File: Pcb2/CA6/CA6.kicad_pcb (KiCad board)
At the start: 2 copper layers, 81.3 x 134.6 mm, 115 parts, among them J1 MICRO_USB, J2 BAT_CON, J3 MODULE_0, J4 MODULE_2, J5 MODULE_1, J6 AUX, J7 AUX, J8 MODULE_3, P1 JTAG, P2 RFD22301 Breakout, Q1 BSS138P, Q10 BSS138P, Q11 BSS138P, Q12 BSS138P, Q13 BSS138P, Q14 BSS138P, Q15 BSS138P, Q16 BSS138P, Q2 BSS138P, Q3 BSS138P, Q4 BSS138P, Q5 BSS138P, Q6 BSS138P, Q7 BSS138P, Q8 BSS138P, Q9 BSS138P, SW1 ERASE, SW2 USB/BATTERY, SW3 RESET, U12 VREG_33, U14 EEPROM, U15 L_PIPE, U16 ATSAM3X8EA-AU_LQFP-144, U17 RFD22301, X1 HOLE, X2 HOLE, X3 HOLE, X7 CRYSTAL_4, X8 32khz

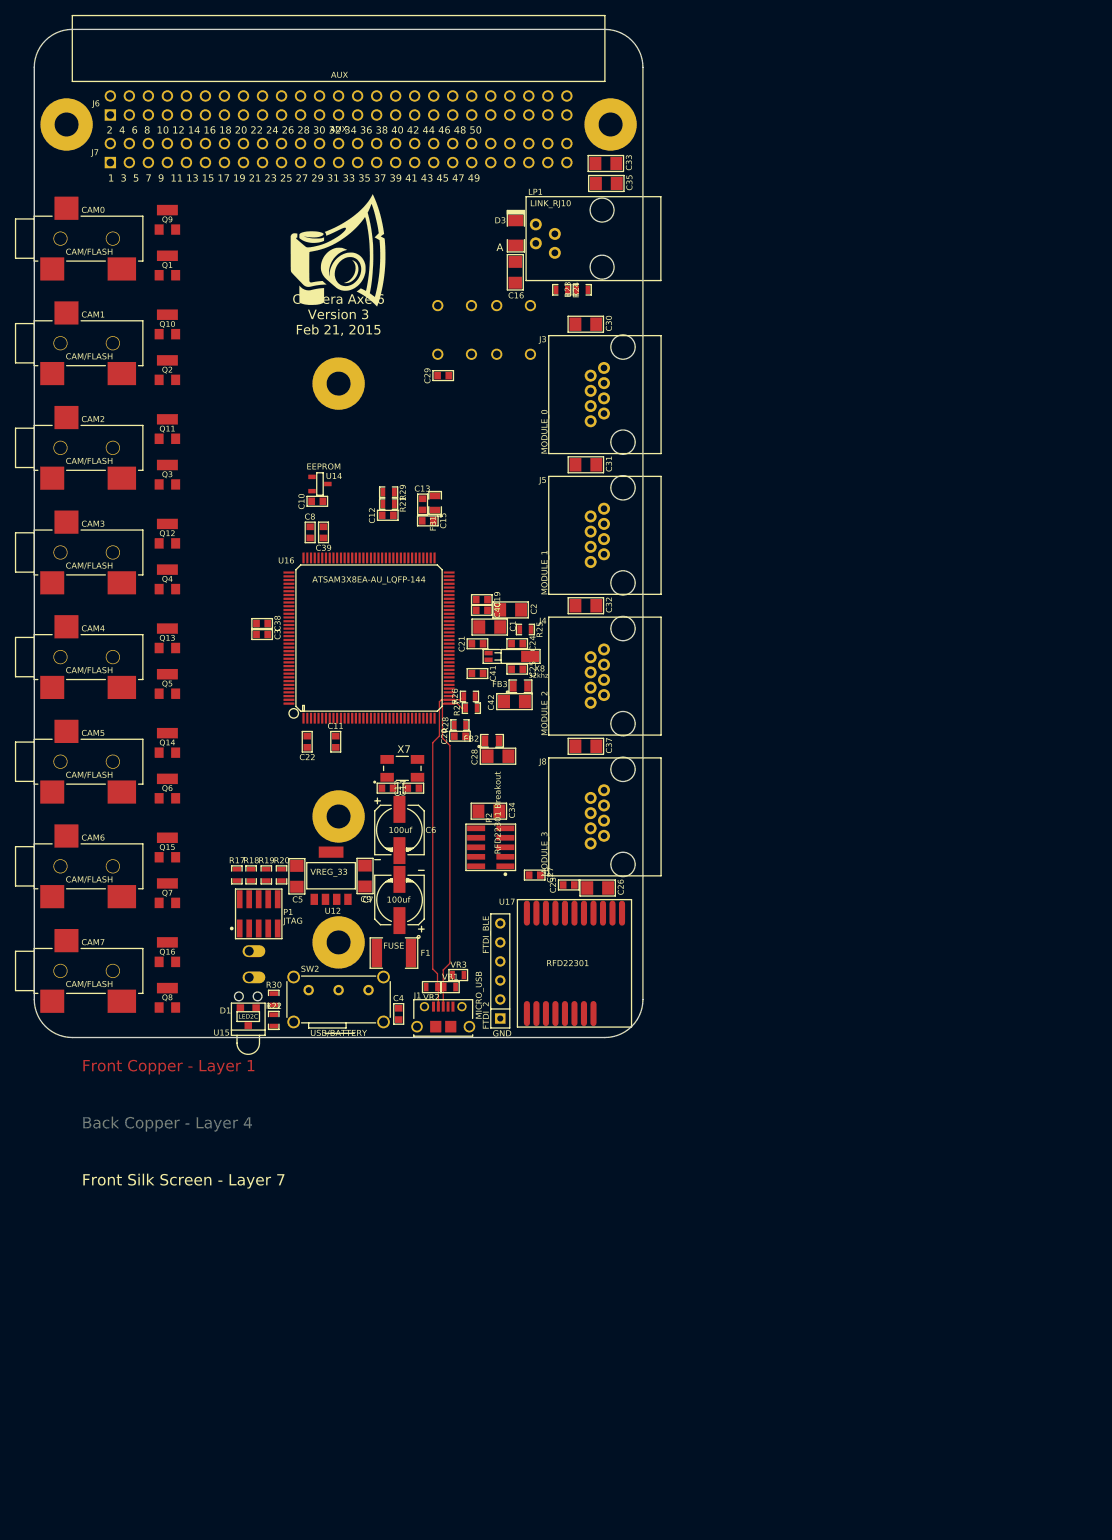
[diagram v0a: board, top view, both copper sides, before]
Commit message: Remove link port, only support 3.3V on aux, make board bigger, make board 2 layers, add camera port leds
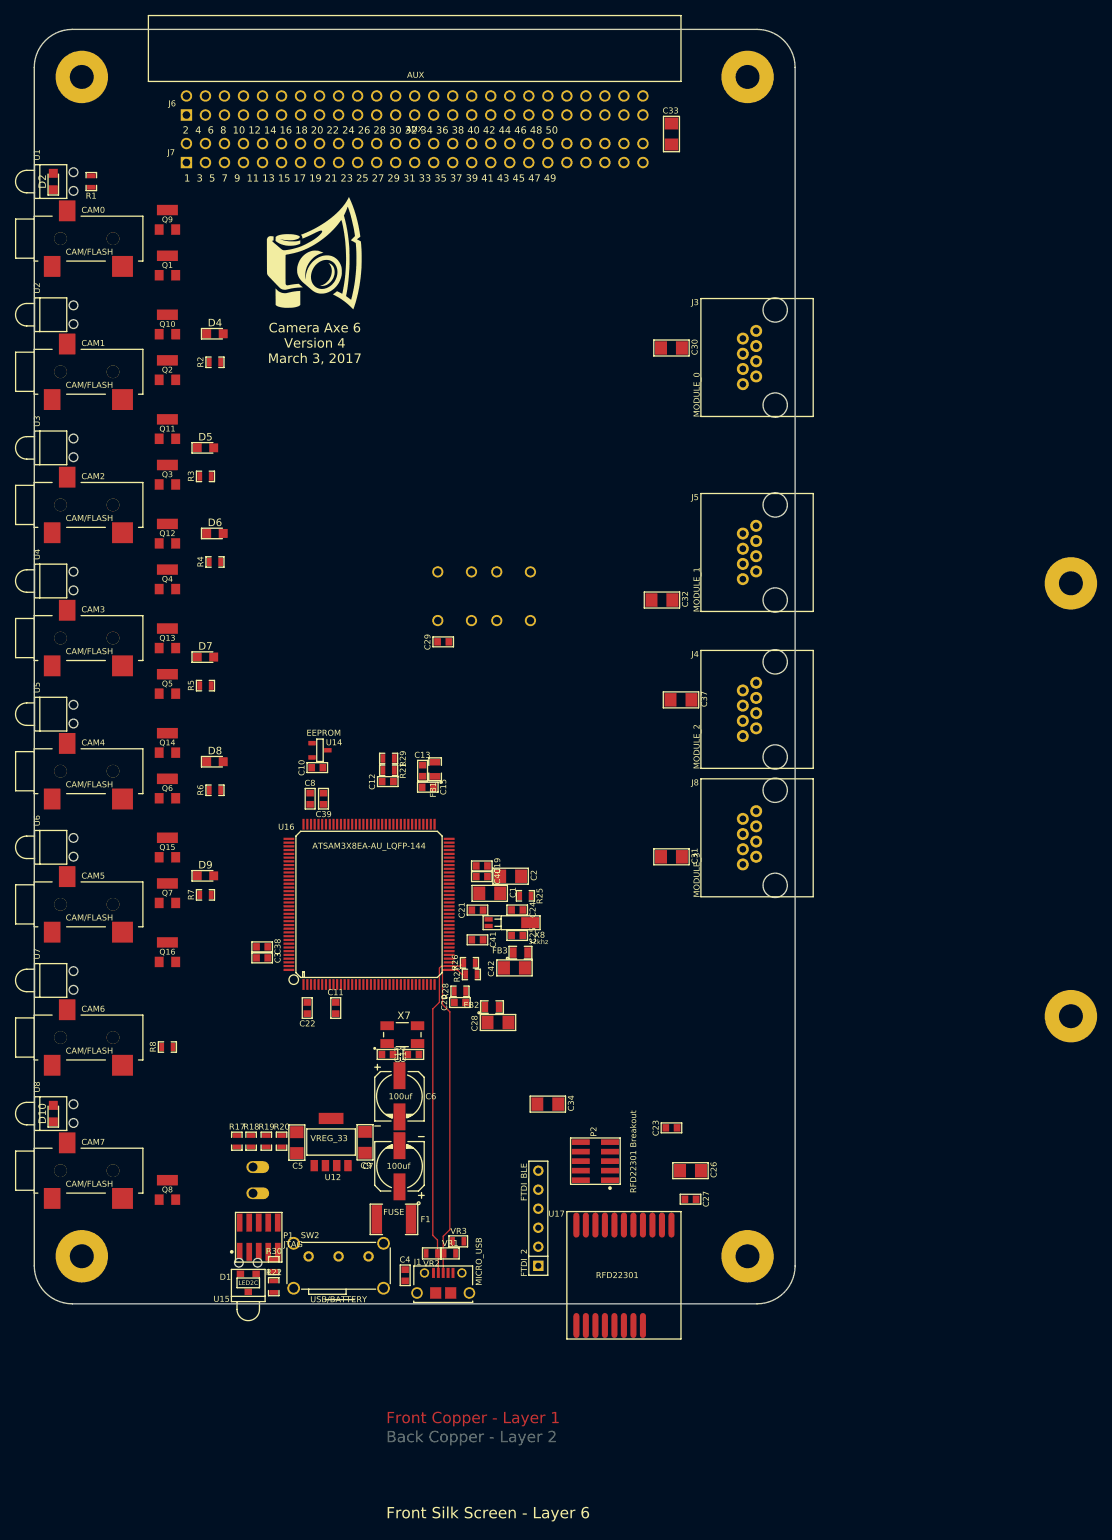
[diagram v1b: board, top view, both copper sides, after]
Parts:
- removed C16, C35: 10uf, CA6:c_1206
- removed D3: SCH_D, CA6:SM1206-D-A
- removed LP1: LINK_RJ10, CA6:RJ10_A-2004-3-4-LP-N-R
- removed R23, R24: 10k, CA6:SM0603_Resistor
- added D10: LED, LEDs:LED_0805, F.Cu at (27.9, 170.2)
- added D2: LED, LEDs:LED_0805, F.Cu at (27.9, 45.7)
- added D4: LED, LEDs:LED_0805, F.Cu at (49.5, 66.0)
- added D5: LED, LEDs:LED_0805, F.Cu at (48.3, 81.3)
- added D6: LED, LEDs:LED_0805, F.Cu at (49.5, 92.7)
- added D7: LED, LEDs:LED_0805, F.Cu at (48.3, 109.2)
- added D8: LED, LEDs:LED_0805, F.Cu at (49.5, 123.2)
- added D9: LED, LEDs:LED_0805, F.Cu at (48.3, 138.4)
- added R1: 680R, CA6:SM0603_Resistor, F.Cu at (33.0, 45.7)
- added R2: 680R, CA6:SM0603_Resistor, F.Cu at (49.5, 69.8)
- added R3: 680R, CA6:SM0603_Resistor, F.Cu at (48.3, 85.1)
- added R4: 680R, CA6:SM0603_Resistor, F.Cu at (49.5, 96.5)
- added R5: 680R, CA6:SM0603_Resistor, F.Cu at (48.3, 113.0)
- added R6: 680R, CA6:SM0603_Resistor, F.Cu at (49.5, 127.0)
- added R7: 680R, CA6:SM0603_Resistor, F.Cu at (48.3, 141.0)
- added R8: 680R, CA6:SM0603_Resistor, F.Cu at (43.2, 161.3)
- added U1: L_PIPE, CA6:SLP3-150-100-R, F.Cu at (27.9, 45.7)
- added U2: L_PIPE, CA6:SLP3-150-100-R, F.Cu at (27.9, 63.5)
- added U3: L_PIPE, CA6:SLP3-150-100-R, F.Cu at (27.9, 81.3)
- added U4: L_PIPE, CA6:SLP3-150-100-R, F.Cu at (27.9, 99.1)
- added U5: L_PIPE, CA6:SLP3-150-100-R, F.Cu at (27.9, 116.8)
- added U6: L_PIPE, CA6:SLP3-150-100-R, F.Cu at (27.9, 134.6)
- added U7: L_PIPE, CA6:SLP3-150-100-R, F.Cu at (27.9, 152.4)
- added U8: L_PIPE, CA6:SLP3-150-100-R, F.Cu at (27.9, 170.2)
- added X4: HOLE, CA6:HOLE_3.0mm, F.Cu at (120.7, 189.2)
- LOGO2: footprint CA6:CA_Logo_Mirror_15mm -> CA6:CA_Logo_15mm
- moved BT1 101.4 mm to (163.8, 128.3)
- moved X3 54.2 mm to (31.8, 189.2)
- moved C31 53.6 mm to (110.5, 135.9)
- moved C27 48.0 mm to (113.0, 181.6)
- moved P2 44.2 mm to (100.3, 176.5)
- moved P1 43.2 mm to (55.4, 186.7)
- moved C3 43.2 mm to (55.8, 149.4)
- moved C38 43.2 mm to (55.8, 147.9)
- moved U17 42.2 mm to (111.8, 191.8)
- moved C34 39.9 mm to (94.0, 168.9)
- moved C26 39.7 mm to (113.0, 177.8)
- moved C21 35.6 mm to (84.6, 143.0)
- moved R26 35.6 mm to (83.5, 150.0)
- moved R28 35.6 mm to (82.2, 153.8)
- moved X7 35.6 mm to (74.5, 159.6)
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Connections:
- J6 pad 48: 5V -> 3V3
- J7 pad 48: 5V -> 3V3
- U16 pad 59: /LP_FOCUS -> (no net)
- U16 pad 60: /LP_SHUTTER -> (no net)
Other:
- board size 81.3 x 134.6 mm -> 101.6 x 170.2 mm
- board text added: "Back Copper - Layer 2"
- board text added: "Back Silk Screen - Layer 5"
- board text added: "Back Solder Mask - Layer 7"
- board text added: "Back Solder Paste - Layer 3"
- board text added: "Board Edge Cut - Layer 12"
- board text added: "Camera Axe 6 Version 4 March 3, 2017"
- board text added: "Front Silk Screen - Layer 6"
- board text added: "Front Solder Mask - Layer 8"
- board text added: "Front Solder Paste - Layer 4"
- board text removed: "Back Copper - Layer 4"
- board text removed: "Back Silk Screen - Layer 8"
- board text removed: "Back Solder Mask - Layer 10"
- board text removed: "Back Solder Paste - Layer 6"
- board text removed: "Board Edge Cut - Layer 11"
- board text removed: "Camera Axe 6 Version 3 Feb 21, 2015"
- board text removed: "Front Silk Screen - Layer 7"
- board text removed: "Front Solder Mask - Layer 9"
- board text removed: "Front Solder Paste - Layer 5"
- board text removed: "GND"

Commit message: Lots more small changes to the pcb
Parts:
- removed BT1: 4xAA_BATTERY_HOLDER, CA6:BATTERY_4AA_12BH348-GR
- removed C26: 10uf, CA6:c_1206
- removed C27: 0.1uf, CA6:c_0603
- removed FTDI_2: FTDI_BLE, CA6:SIL-6
- removed U17: RFD22301, CA6:RFD22301
- P2: footprint CA6:JTAG_20021121-00010C4LF -> Socket_Strips:Socket_Strip_Straight_2x05_Pitch2.54mm
- moved SW3 74.3 mm to (123.2, 162.6)
- moved D1 74.0 mm to (124.5, 170.2), turned to 0 degrees
- moved U15 74.0 mm to (124.5, 170.2), turned to 90 degrees
- moved R22 69.8 mm to (124.5, 174.0), turned to 90 degrees
- moved R30 66.6 mm to (121.9, 174.0), turned to 90 degrees
- moved C29 63.1 mm to (118.1, 157.5), turned to 270 degrees
- moved SW1 62.5 mm to (123.2, 153.7)
- moved Q7 25.7 mm to (41.9, 165.1)
- moved D9 24.7 mm to (27.9, 152.4), turned to 90 degrees
- moved D8 24.4 mm to (27.9, 134.6), turned to 90 degrees
- moved Q16 22.9 mm to (41.9, 170.2)
- moved D6 22.5 mm to (27.9, 99.1), turned to 90 degrees
- moved Q6 21.9 mm to (41.9, 147.3)
- moved D4 21.7 mm to (27.9, 63.5), turned to 90 degrees
- moved D7 21.7 mm to (27.9, 116.8), turned to 90 degrees
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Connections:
- C23 pad 1: GND -> 3V3
- C23 pad 2: 3V3 -> GND
- C34 pad 1: GND -> 3V3
- C34 pad 2: 3V3 -> GND
- P2 pad 1: /BLE_TX -> GND
- P2 pad 10: GND -> (no net)
- P2 pad 2: /BLE_RX -> 3V3
- P2 pad 3: /BLE_RTS -> /CC_RX
- P2 pad 4: /BLE_CTS -> Net-(P2-Pad4)
- P2 pad 5: /BLE_GPIO4 -> /CC_TX
- P2 pad 6: /BLE_GPIO5 -> Net-(P2-Pad6)
- P2 pad 7: /BLE_GPIO6 -> /CC_RTS
- P2 pad 8: 3V3 -> (no net)
- P2 pad 9: GND -> /CC_CTS
- R22 pad 1: Net-(R22-Pad1) -> Net-(P2-Pad6)
- R30 pad 1: Net-(R30-Pad1) -> Net-(P2-Pad4)
- U16 pad 13: Net-(R22-Pad1) -> (no net)
- U16 pad 14: Net-(R30-Pad1) -> (no net)
- U16 pad 5: /BLE_RX -> /CC_RX
- U16 pad 6: /BLE_TX -> /CC_TX
- U16 pad 7: /BLE_RTS -> /CC_RTS
- U16 pad 8: /BLE_CTS -> /CC_CTS
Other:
- board text removed: "+"
- board text removed: "-"
- board text removed: "BLACK"
- board text removed: "RED"

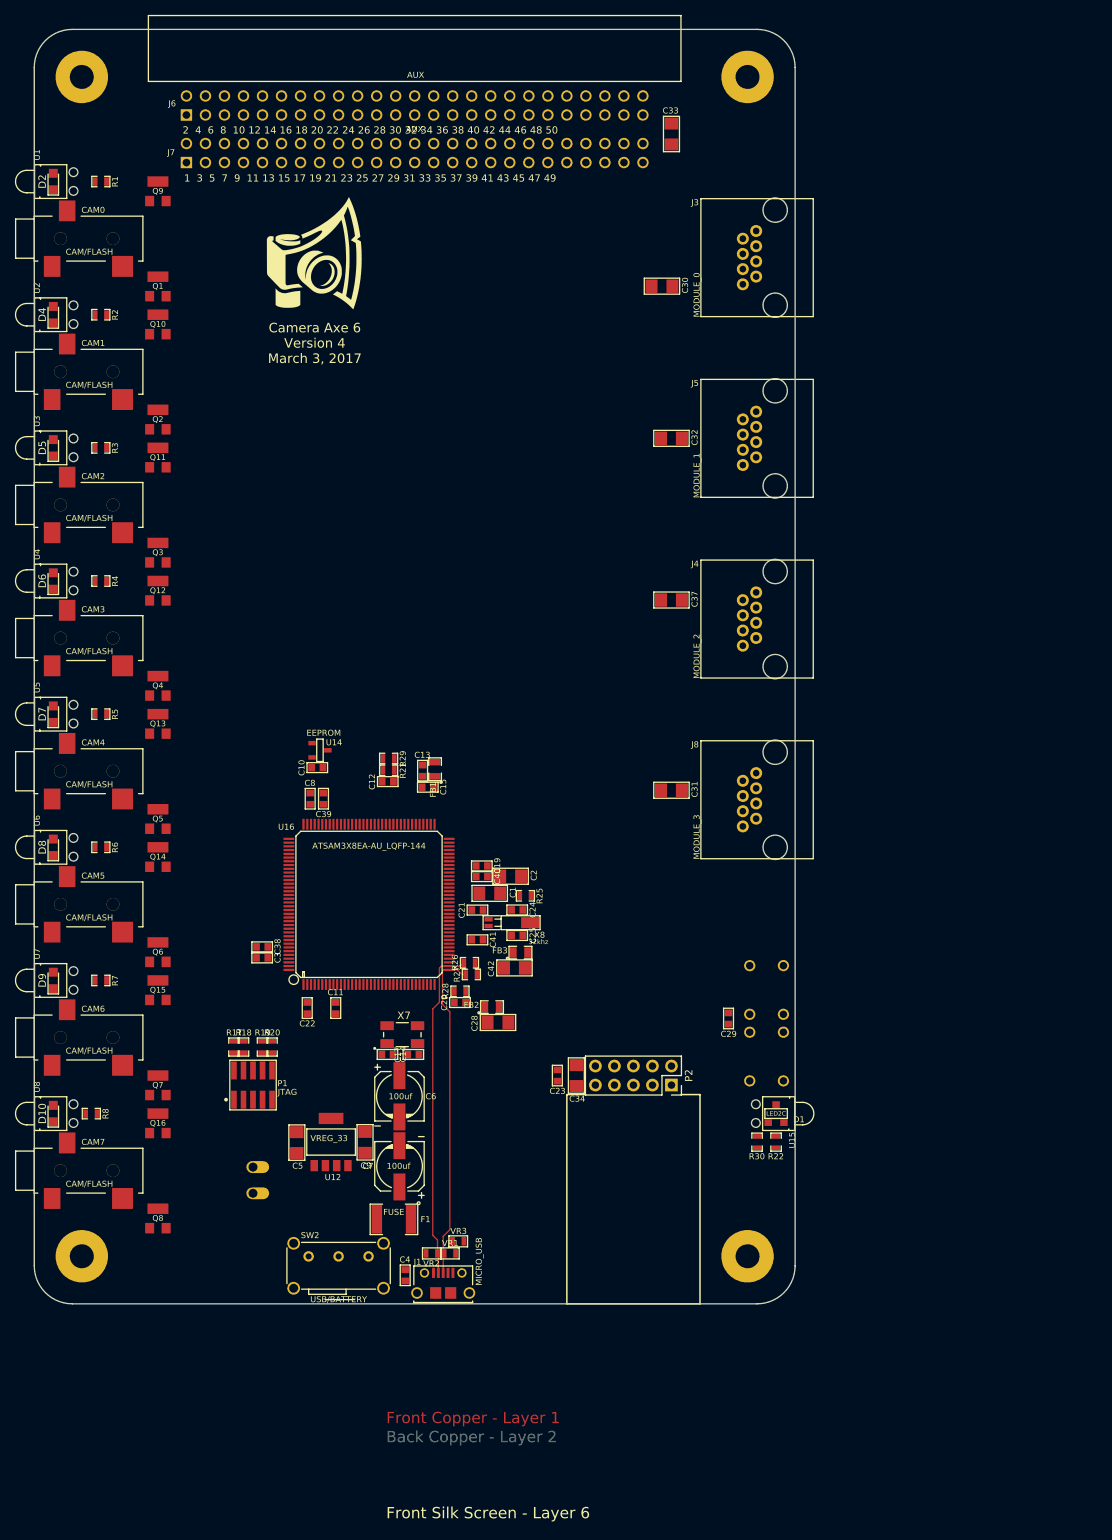
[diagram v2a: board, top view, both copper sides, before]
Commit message: Clean up layout and add ground plane
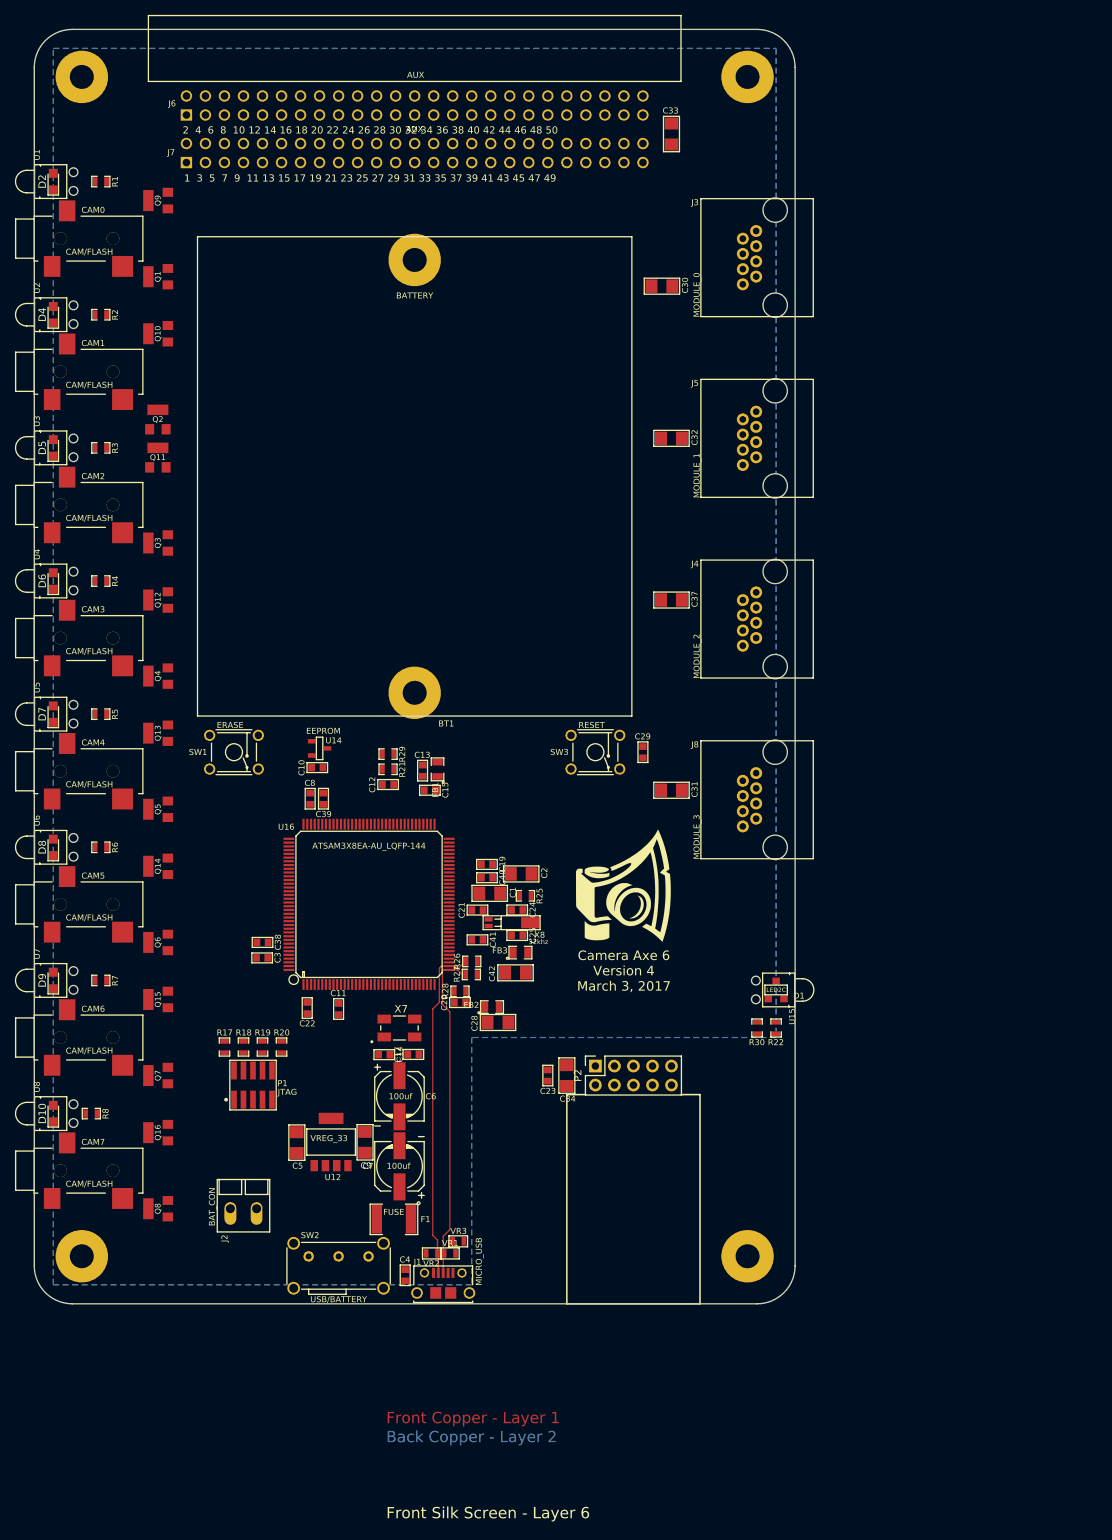
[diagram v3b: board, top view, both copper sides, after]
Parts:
- added BT1: BATTERY, CA6:BATTERY_4AA_12BH348-GR, F.Cu at (76.2, 85.1)
- J2, SW1, SW3: moved to F.Cu
- moved LOGO1 94.0 mm to (104.1, 139.7)
- moved LOGO2 93.7 mm to (104.1, 139.7)
- moved SW1 77.9 mm to (52.1, 121.9), turned to 0 degrees
- moved SW3 46.6 mm to (100.3, 121.9), turned to 0 degrees
- moved C29 37.4 mm to (106.7, 121.9), turned to 90 degrees
- moved D1 16.5 mm to (124.5, 153.7)
- moved U15 16.5 mm to (124.5, 153.7)
- moved R22 15.2 mm to (124.5, 158.8)
- moved R30 15.2 mm to (121.9, 158.8)
- moved P2 10.5 mm to (100.3, 163.8), turned to 90 degrees
- moved J2 4.02 mm to (53.3, 182.9), turned to 180 degrees
- moved Q10 2.84 mm to (40.6, 66.0), turned to 90 degrees
- moved Q9 2.84 mm to (40.6, 48.3), turned to 90 degrees
- moved Q12 2.84 mm to (40.6, 101.6), turned to 90 degrees
- moved Q13 2.84 mm to (40.6, 119.4), turned to 90 degrees
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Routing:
- added copper zone on B.Cu, net GND

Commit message: Minor cleanup
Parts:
- turned C30 to 180 degrees
- turned C31 to 180 degrees
- turned C32 to 180 degrees
- turned C37 to 180 degrees
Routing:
- net GND: track 0.00 -> 179.3 mm, vias 0 -> 69

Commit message: Add more traces
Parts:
- moved C9 10.1 mm to (65.4, 164.8)
- moved C5 9.35 mm to (62.1, 164.8)
- moved C7 2.02 mm to (72.9, 175.6), turned to 180 degrees
- moved U12 1.71 mm to (63.5, 173.2), turned to 180 degrees
- moved C6 1.14 mm to (73.0, 167.9), turned to 180 degrees
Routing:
- net 5V: track 0.00 -> 34.0 mm
- net Net-(J2-Pad2): track 0.00 -> 22.1 mm
- net /VBUS: track 0.00 -> 18.6 mm
- net Net-(C14-Pad1): track 0.00 -> 18.1 mm
- net GND: track 179.3 -> 163.9 mm, vias 69 -> 72
- net 3V3: track 0.00 -> 11.6 mm, vias 0 -> 2
- net Net-(C17-Pad1): track 0.00 -> 11.5 mm, vias 0 -> 2
- net Net-(F1-Pad2): track 0.00 -> 7.15 mm
